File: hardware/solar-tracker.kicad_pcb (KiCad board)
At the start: 2 copper layers, 20 parts, among them J1 12V Power, J2 5V Power, J3 Limit Switch A, J4 Limit Switch B, J5 Serial Communication, J6 microSD Module, J7 RTC Module, J8 STEPPER A, J9 STEPPER B, SW1 SW_Push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

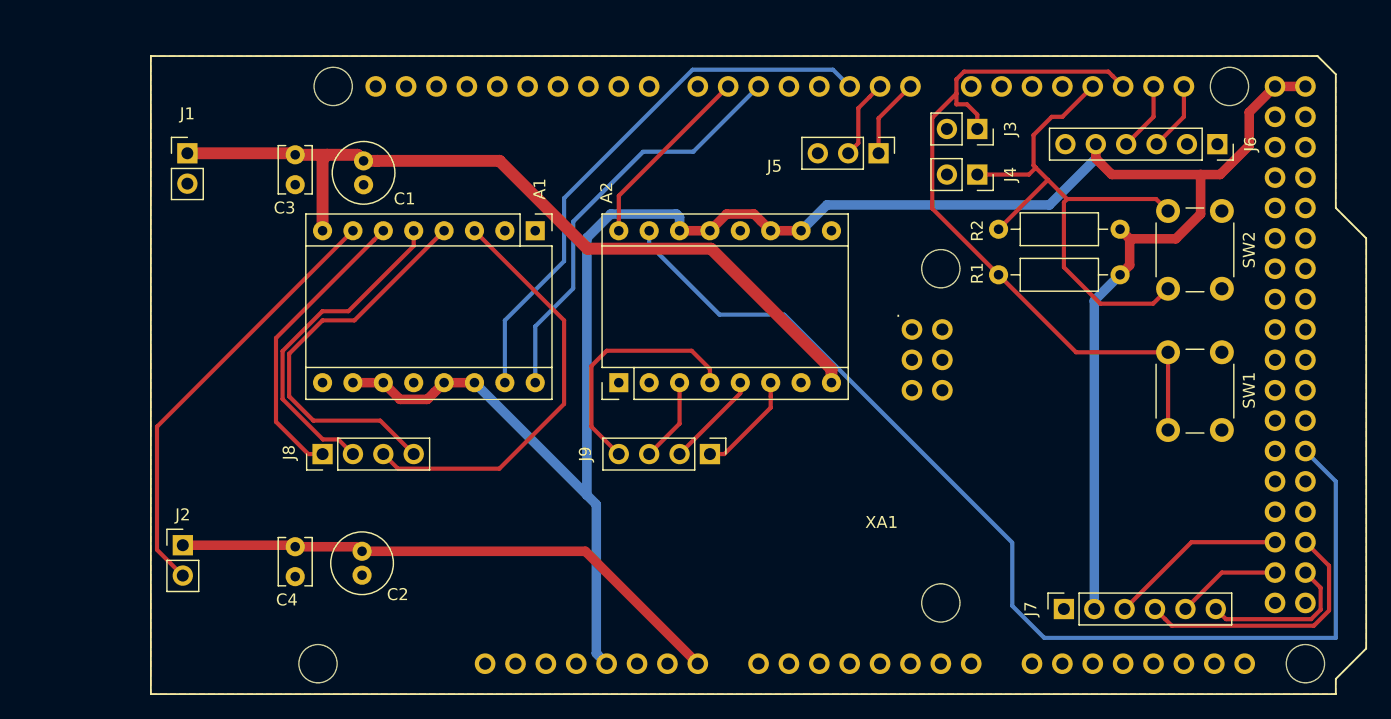
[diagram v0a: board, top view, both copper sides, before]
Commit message: update pcb con agujeros no conductores
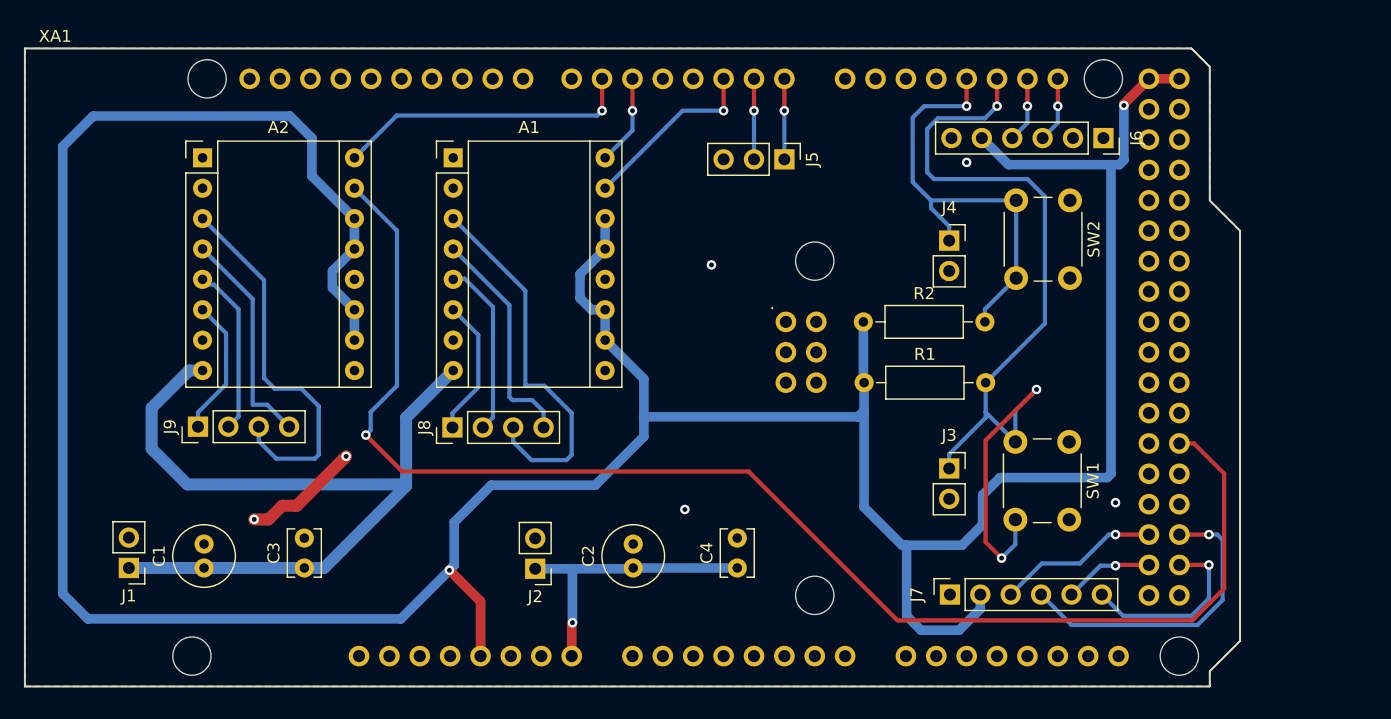
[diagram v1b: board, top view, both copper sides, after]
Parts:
- moved J9 42.9 mm to (107.7, 91.4), turned to 90 degrees
- moved A2 39.5 mm to (108.1, 69.0), turned to 0 degrees
- moved C4 37.0 mm to (152.8, 103.3), turned to 90 degrees
- moved C1 36.6 mm to (108.2, 103.3), turned to 90 degrees
- moved J1 35.0 mm to (101.9, 103.3), turned to 180 degrees
- moved C3 34.6 mm to (116.6, 103.3), turned to 90 degrees
- moved J2 29.5 mm to (135.9, 103.3), turned to 180 degrees
- moved J3 28.5 mm to (170.5, 94.9), turned to 0 degrees
- moved R1 23.2 mm to (163.4, 87.8), turned to 0 degrees
- moved R2 22.8 mm to (163.3, 82.7), turned to 0 degrees
- moved C2 22.7 mm to (144.1, 103.3), turned to 90 degrees
- moved SW1 14.8 mm to (180.5, 92.7)
- moved SW2 12.7 mm to (180.6, 72.5)
- moved J8 11.1 mm to (129.0, 91.5)
- moved XA1 10.6 mm to (93.2, 113.2)
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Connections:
- C1 pad 2: GNDD -> GND
- C2 pad 2: GND -> GNDD
- C3 pad 2: GNDD -> GND
- C4 pad 2: GND -> GNDD
- J1 pad 2: GNDD -> GND
- J2 pad 2: GND -> GNDD
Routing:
- net +5V: track 177.7 -> 292.1 mm, vias 0 -> 2
- net Net-(A1-Pad15): track 46.4 -> 15.3 mm, vias 0 -> 1
- net Net-(A1-Pad16): track 35.0 -> 7.55 mm, vias 0 -> 1
- net GND: track 36.5 -> 9.87 mm, vias 0 -> 2
- net Net-(A2-Pad3): track 7.02 -> 32.0 mm
- net Net-(A2-Pad15): track 91.9 -> 116.9 mm, vias 0 -> 1
- net VIN: track 47.2 -> 24.2 mm, vias 0 -> 1
- net Net-(J3-Pad1): track 61.7 -> 78.0 mm, vias 0 -> 3
- net Net-(A1-Pad4): track 33.2 -> 19.0 mm
- net Net-(A1-Pad6): track 24.7 -> 11.6 mm
- net Net-(A1-Pad5): track 27.7 -> 14.8 mm
- net Net-(J4-Pad1): track 49.3 -> 37.1 mm, vias 0 -> 1
- net Net-(A2-Pad16): track 15.9 -> 25.0 mm, vias 0 -> 1
- net Net-(A2-Pad5): track 8.07 -> 14.2 mm
- net Net-(A1-Pad3): track 35.4 -> 31.7 mm
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- added copper zone on B.Cu, net GND
- added copper zone on F.Cu, net GNDD
- removed copper zone on F.Cu, net GND
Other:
- board outline added: 101.6 x 53.3 mm
- net class DIG_GND added: clearance 0.2, trace_width 0.8, via_dia 0.8, via_drill 0.4
- net class MOT_GND added: clearance 0.2, trace_width 1, via_dia 0.8, via_drill 0.4

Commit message: update pcb pistas más anchas
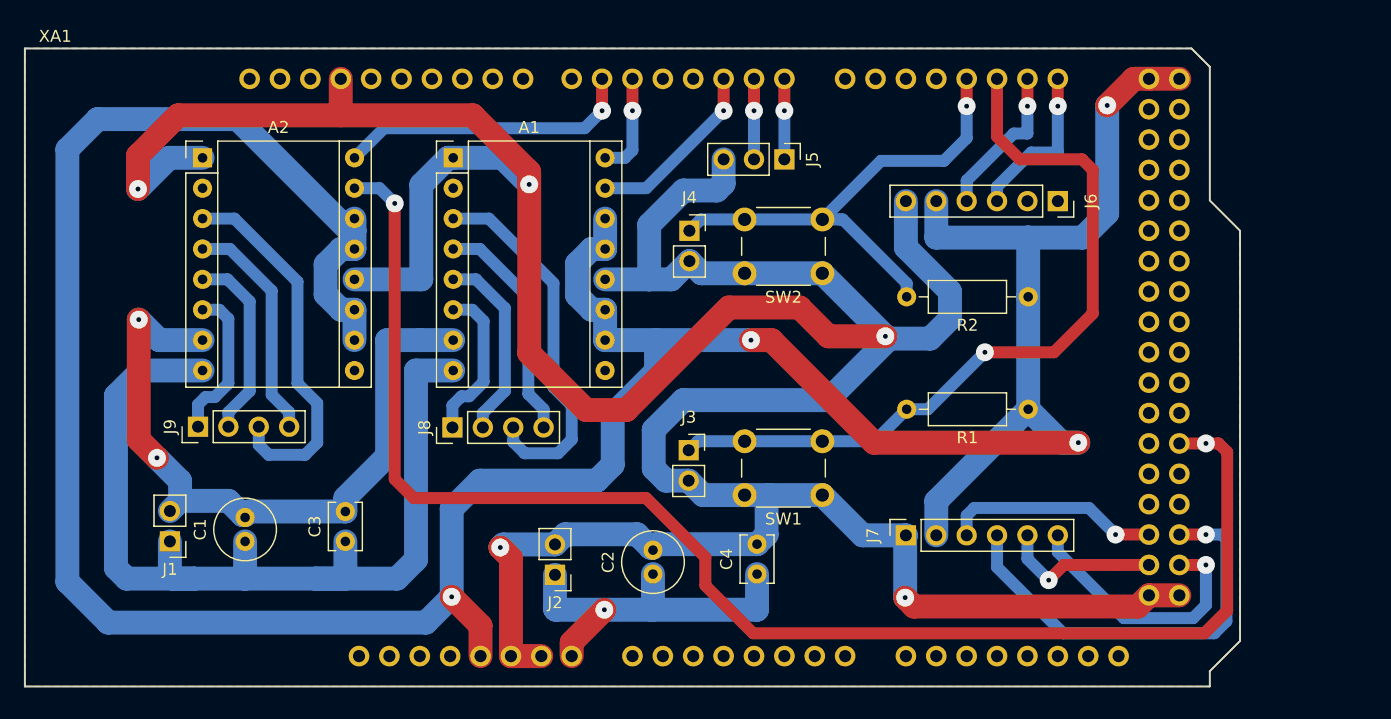
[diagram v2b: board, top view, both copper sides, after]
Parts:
- moved J3 21.8 mm to (148.7, 93.4)
- moved J4 21.7 mm to (148.8, 75.1)
- moved SW2 21.6 mm to (159.9, 78.6), turned to 180 degrees
- moved SW1 21.1 mm to (159.9, 97.2), turned to 180 degrees
- moved R2 13.9 mm to (177.1, 80.6), turned to 180 degrees
- moved R1 13.9 mm to (177.1, 90.0), turned to 180 degrees
- moved J6 6.50 mm to (179.6, 72.6)
- moved J7 6.17 mm to (166.9, 100.5)
- moved C1 4.09 mm to (111.6, 101.0)
- moved C3 4.09 mm to (120.0, 101.0)
- moved J1 4.09 mm to (105.3, 101.0)
- moved J2 1.73 mm to (137.5, 103.8)
- moved C2 1.73 mm to (145.7, 103.8)
- moved C4 1.73 mm to (154.4, 103.8)
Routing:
- net GNDD: track 0.00 -> 300.0 mm, vias 4 -> 5
- net GND: track 9.87 -> 59.6 mm
- net +5V: track 292.1 -> 277.3 mm, vias 2 -> 4
- net Net-(J3-Pad1): track 78.0 -> 64.5 mm, vias 3 -> 1
- net +12V: track 68.8 -> 81.2 mm
- net Net-(J7-Pad4): track 25.9 -> 35.5 mm
- net Net-(J6-Pad3): track 5.48 -> 13.6 mm
- net Net-(J6-Pad4): track 5.48 -> 13.0 mm
- net VIN: track 24.2 -> 30.9 mm
- net Net-(J7-Pad6): track 15.6 -> 22.1 mm
- net Net-(J7-Pad5): track 7.50 -> 13.5 mm
- net Net-(A2-Pad15): track 116.9 -> 121.6 mm, vias 1 -> 2
- net Net-(J4-Pad1): track 37.1 -> 41.7 mm
- net Net-(J7-Pad3): track 13.6 -> 18.1 mm
- net Net-(A2-Pad5): track 14.2 -> 16.5 mm
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- removed copper zone on B.Cu, net GND
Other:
- net class DIG_GND: trace_width 0.8 -> 2; via_dia 0.8 -> 1.5
- net class DIG_PWR: trace_width 0.8 -> 2; via_dia 0.8 -> 1.5
- net class Default: trace_width 0.35 -> 1; via_dia 0.8 -> 1.5
- net class MOT_GND: trace_width 1 -> 2; via_dia 0.8 -> 1.5
- net class MOT_PWR: trace_width 1 -> 2; via_dia 0.8 -> 1.5

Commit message: new pcb iteration more C other power conn
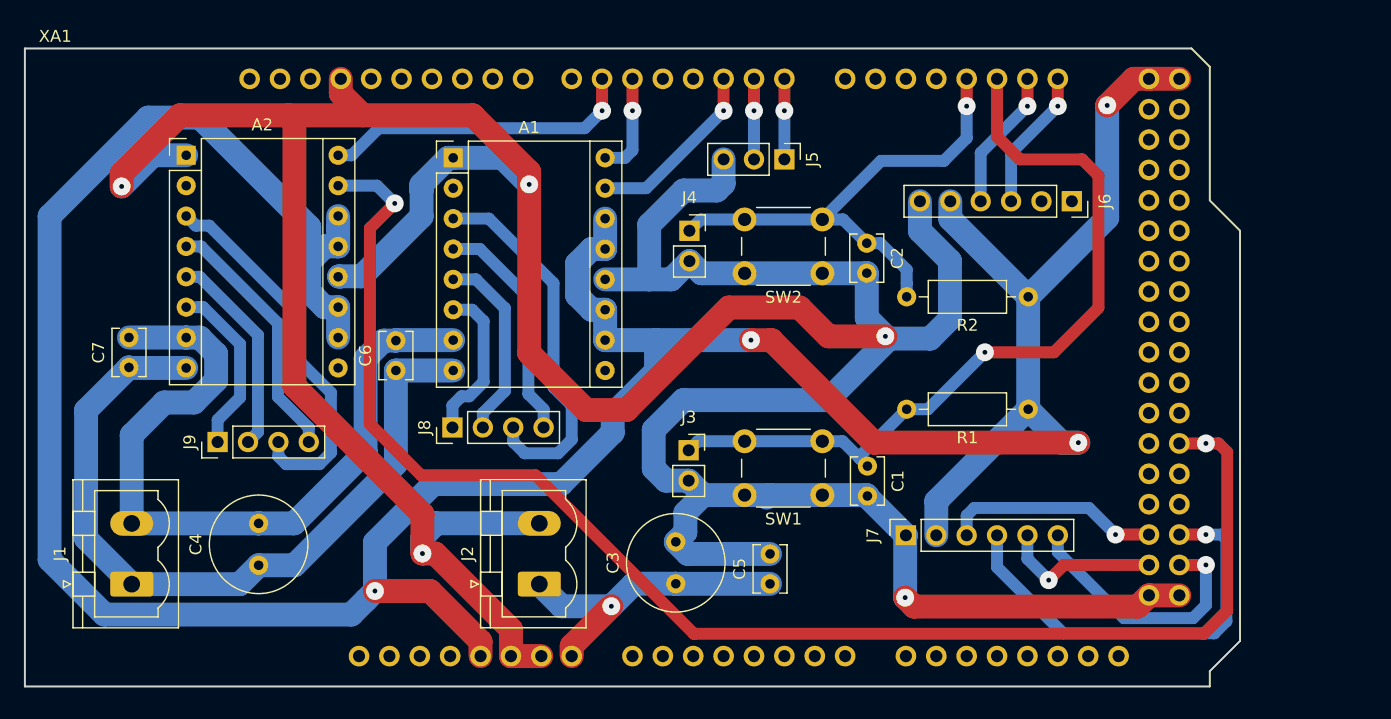
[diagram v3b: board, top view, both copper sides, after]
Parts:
- added C5: 0.1uF, Capacitor_THT:C_Disc_D3.8mm_W2.6mm_P2.50mm, F.Cu at (155.5, 104.6)
- added C6: 0.1uF, Capacitor_THT:C_Disc_D3.8mm_W2.6mm_P2.50mm, F.Cu at (124.2, 86.7)
- added C7: 0.1uF, Capacitor_THT:C_Disc_D3.8mm_W2.6mm_P2.50mm, F.Cu at (101.9, 86.5)
- C1, C2: value 100uF -> 0.1uF; footprint Capacitor_THT:C_Radial_D5.0mm_H11.0mm_P2.00mm -> Capacitor_THT:C_Disc_D3.8mm_W2.6mm_P2.50mm
- C3, C4: value 0.1uF -> 100uF; footprint Capacitor_THT:C_Disc_D3.8mm_W2.6mm_P2.50mm -> Capacitor_THT:C_Radial_D8.0mm_H11.5mm_P3.50mm
- J1, J2: footprint Connector_PinHeader_2.54mm:PinHeader_1x02_P2.54mm_Vertical -> Connector_Phoenix_MSTB:PhoenixContact_MSTBVA_2,5_2-G-5,08_1x02_P5.08mm_Vertical
- moved C1 52.4 mm to (163.7, 94.7), turned to 270 degrees
- moved C4 41.7 mm to (112.8, 103.0)
- moved C2 32.9 mm to (163.6, 76.1), turned to 270 degrees
- moved C3 27.9 mm to (147.6, 104.6)
- moved J1 4.79 mm to (102.2, 104.6), turned to 90 degrees
- moved J9 2.08 mm to (109.3, 92.7)
- moved J2 1.52 mm to (136.2, 104.6), turned to 90 degrees
- moved A2 1.38 mm to (106.7, 68.7)
- moved J6 1.17 mm to (180.8, 72.6)
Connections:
- net Net-(A1-Pad15) renamed STEP_A
- net Net-(A1-Pad16) renamed DIR_A
- net Net-(A2-Pad15) renamed STEP_B
- net Net-(A2-Pad16) renamed DIR_B
- A1 pad 8: +12V -> VMOT_A
- A2 pad 8: +12V -> VMOT_A
- C1 pad 1: +12V -> LIM_A
- C1 pad 2: GND -> GNDD
- C2 pad 1: VIN -> LIM_B
- C3 pad 1: +12V -> VIN
- C3 pad 2: GND -> GNDD
- C4 pad 1: VIN -> VMOT_A
- C4 pad 2: GNDD -> GND
- J1 pad 1: +12V -> VMOT_A
- J3 pad 1: Net-(J3-Pad1) -> LIM_A
- J4 pad 1: Net-(J4-Pad1) -> LIM_B
- R1 pad 2: Net-(J3-Pad1) -> LIM_A
- R2 pad 2: Net-(J4-Pad1) -> LIM_B
- SW1 pad 2: Net-(J3-Pad1) -> LIM_A
- SW2 pad 2: Net-(J4-Pad1) -> LIM_B
- XA1 pad D18: Net-(J4-Pad1) -> LIM_B
- XA1 pad D19: Net-(J3-Pad1) -> LIM_A
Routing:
- net +12V: track 81.2 -> 0.00 mm
- net LIM_A: track 0.00 -> 67.1 mm, vias 0 -> 1
- net VMOT_A: track 0.00 -> 64.8 mm
- net Net-(J3-Pad1): track 64.5 -> 0.00 mm, vias 1 -> 0
- net GNDD: track 300.0 -> 343.1 mm
- net LIM_B: track 0.00 -> 42.4 mm, vias 0 -> 1
- net Net-(J4-Pad1): track 41.7 -> 0.00 mm, vias 1 -> 0
- net GND: track 59.6 -> 64.2 mm, vias 2 -> 0
- net VIN: track 30.9 -> 26.4 mm
- net +5V: track 277.3 -> 274.1 mm
- net Net-(A2-Pad4): track 19.2 -> 21.3 mm
- net Net-(J6-Pad3): track 13.6 -> 11.9 mm
- net Net-(A2-Pad6): track 13.0 -> 14.7 mm
- net Net-(A2-Pad5): track 16.5 -> 17.9 mm
- net DIR_B: track 25.0 -> 26.3 mm
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- removed copper zone on B.Cu, net GNDD
- removed copper zone on F.Cu, net GNDD
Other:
- net class DIG_GND: clearance 0.2 -> 0.5
- net class DIG_PWR: clearance 0.2 -> 0.5
- net class Default: clearance 0.2 -> 0.5
- net class MOT_GND: clearance 0.2 -> 0.5
- net class MOT_PWR: clearance 0.2 -> 0.5
- rule trace_clearance: 0.2 -> 0.5
